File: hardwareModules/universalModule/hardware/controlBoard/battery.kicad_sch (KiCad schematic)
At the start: 36 parts, among them Q1 AONR21357, Q2 AONR21357, Q3 2N7002, U10 TP5100, U4 SD8942, U9 PIEZO

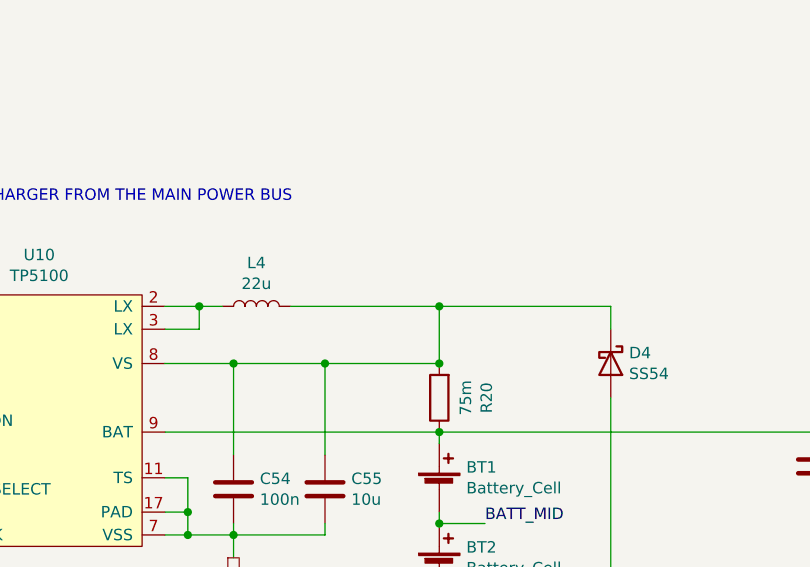
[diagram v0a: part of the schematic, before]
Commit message: um: Fix hardware bugs, prepare v0.5
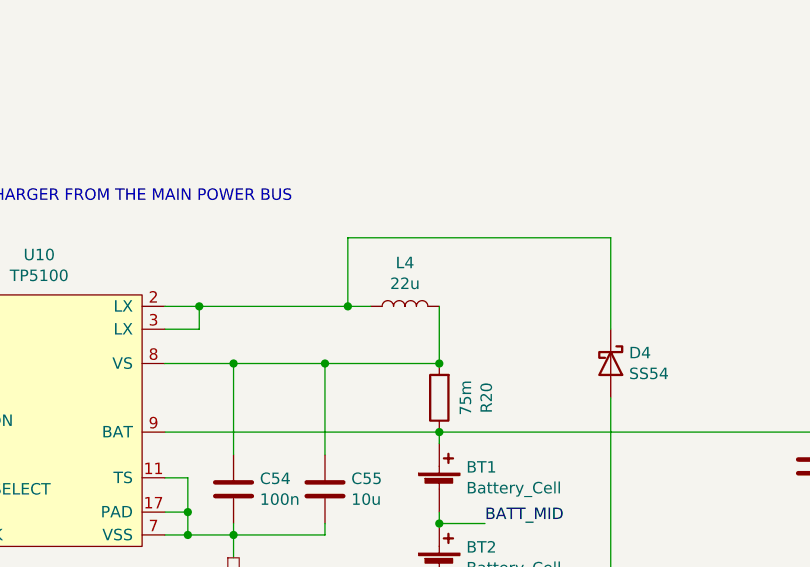
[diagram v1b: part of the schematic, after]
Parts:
- U4: JLCPCB_CORRECTION 0;0;180 -> 0;0;-90
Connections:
- net at L4.1, U10.2 (LX), U10.3 (LX): now also D4.1 (K)
- net at C54.1, C55.1, L4.2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: no longer D4.1 (K)
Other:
- moved on the sheet: L4
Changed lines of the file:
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@@
 (kicad_sch (version 20211123) (generator eeschema)
   (paper "A4")
-  (junction (at 130.81 81.28) (diameter 0) (color 0 0 0 0)
-  )
   (junction (at 104.14 81.28) (diameter 0) (color 0 0 0 0)
   )
@@
   )
   (junction (at 130.81 105.41) (diameter 0) (color 0 0 0 0)
+  )
+  (junction (at 120.65 81.28) (diameter 0) (color 0 0 0 0)
   )
   (junction (at 130.81 118.11) (diameter 0) (color 0 0 0 0)
@@
     (stroke (width 0) (type default) (color 0 0 0 0))
   )
-  (wire (pts (xy 149.86 81.28) (xy 149.86 83.82))
+  (wire (pts (xy 149.86 73.66) (xy 149.86 83.82))
     (stroke (width 0) (type default) (color 0 0 0 0))
   )
@@
     (stroke (width 0) (type default) (color 0 0 0 0))
   )
-  (wire (pts (xy 114.3 81.28) (xy 130.81 81.28))
-    (stroke (width 0) (type default) (color 0 0 0 0))
-  )
   (wire (pts (xy 220.98 44.45) (xy 242.57 44.45))
     (stroke (width 0) (type default) (color 0 0 0 0))
@@
     (stroke (width 0) (type default) (color 0 0 0 0))
   )
-  (wire (pts (xy 104.14 81.28) (xy 106.68 81.28))
+  (wire (pts (xy 104.14 81.28) (xy 120.65 81.28))
     (stroke (width 0) (type default) (color 0 0 0 0))
   )
@@
     (stroke (width 0) (type default) (color 0 0 0 0))
   )
-  (wire (pts (xy 130.81 81.28) (xy 149.86 81.28))
-    (stroke (width 0) (type default) (color 0 0 0 0))
-  )
   (wire (pts (xy 100.33 100.33) (xy 102.87 100.33))
     (stroke (width 0) (type default) (color 0 0 0 0))
@@
     (stroke (width 0) (type default) (color 0 0 0 0))
   )
+  (wire (pts (xy 120.65 73.66) (xy 120.65 81.28))
+    (stroke (width 0) (type default) (color 0 0 0 0))
+  )
   (wire (pts (xy 130.81 113.03) (xy 130.81 114.3))
     (stroke (width 0) (type default) (color 0 0 0 0))
   )
+  (wire (pts (xy 149.86 73.66) (xy 120.65 73.66))
+    (stroke (width 0) (type default) (color 0 0 0 0))
+  )
   (wire (pts (xy 130.81 114.3) (xy 130.81 118.11))
     (stroke (width 0) (type default) (color 0 0 0 0))
@@
   )
   (wire (pts (xy 80.01 162.56) (xy 80.01 165.1))
+    (stroke (width 0) (type default) (color 0 0 0 0))
+  )
+  (wire (pts (xy 120.65 81.28) (xy 123.19 81.28))
     (stroke (width 0) (type default) (color 0 0 0 0))
   )
@@
     (pin "9")
   )
-  (symbol (lib_id "Device:L") (at 110.49 81.28 90) (unit 1)
-    (in_bom yes) (on_board yes)
-    (property "Reference" "L4" (id 0) (at 110.49 76.454 90))
-    (property "Value" "22u" (id 1) (at 110.49 78.7654 90))
-    (property "Footprint" "rofi:SLO0630H" (id 2) (at 110.49 81.28 0)
-      (effects (font (size 1.27 1.27)) hide)
-    )
-    (property "Datasheet" "~" (id 3) (at 110.49 81.28 0)
-      (effects (font (size 1.27 1.27)) hide)
-    )
-    (property "LCSC" "C207843" (id 4) (at 110.49 81.28 90)
+  (symbol (lib_id "Device:L") (at 127 81.28 90) (unit 1)
+    (in_bom yes) (on_board yes)
+    (property "Reference" "L4" (id 0) (at 127 76.454 90))
+    (property "Value" "22u" (id 1) (at 127 78.7654 90))
+    (property "Footprint" "rofi:SLO0630H" (id 2) (at 127 81.28 0)
+      (effects (font (size 1.27 1.27)) hide)
+    )
+    (property "Datasheet" "~" (id 3) (at 127 81.28 0)
+      (effects (font (size 1.27 1.27)) hide)
+    )
+    (property "LCSC" "C207843" (id 4) (at 127 81.28 90)
       (effects (font (size 1.27 1.27)) hide)
     )
@@
       (effects (font (size 1.27 1.27)) hide)
     )
-    (property "JLCPCB_CORRECTION" "0;0;180" (id 5) (at 95.25 154.94 0)
-      (effects (font (size 1.27 1.27)) hide)
-    )
+    (property "JLCPCB_CORRECTION" "0;0;-90" (id 5) (at 95.25 154.94 0)
+      (effects (font (size 1.27 1.27)) hide)
+    )

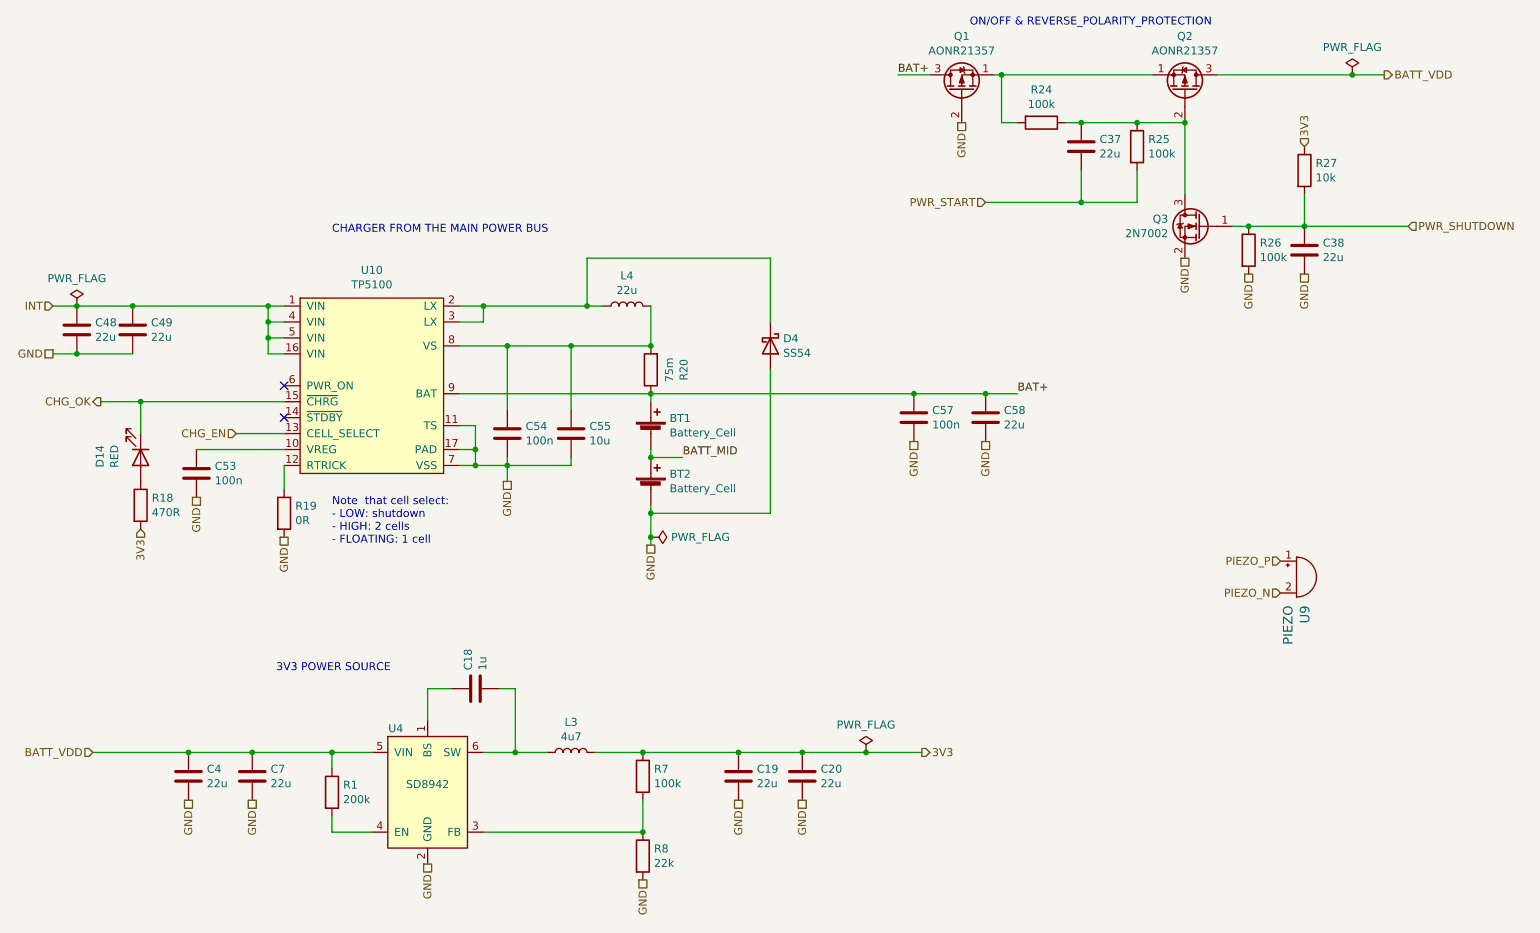
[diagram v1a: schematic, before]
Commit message: hardware: Add custom FPC cables
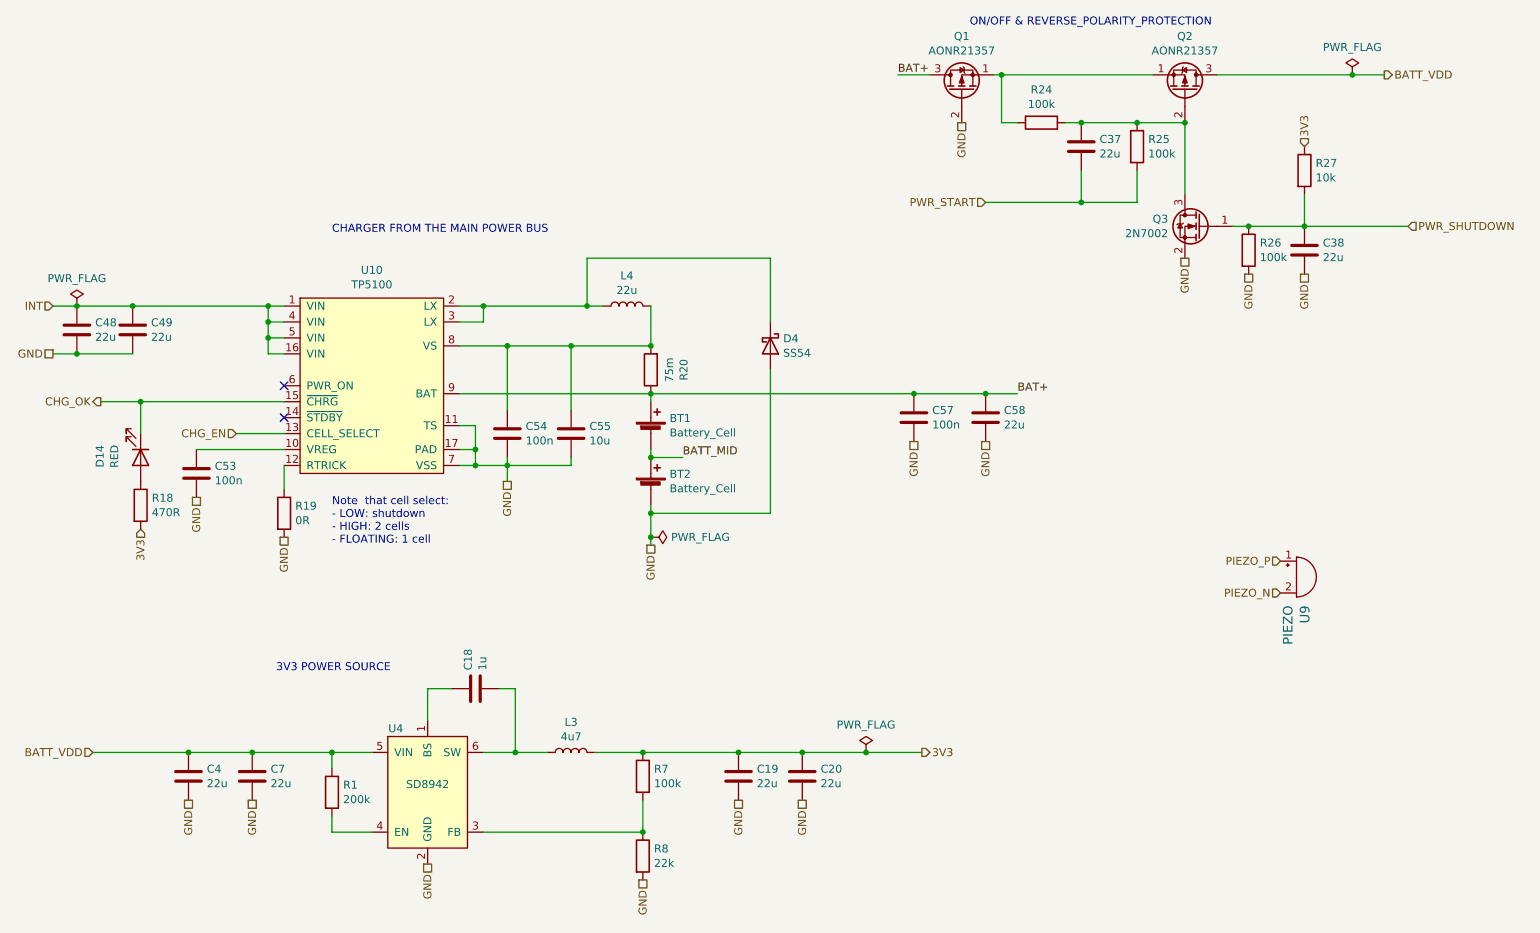
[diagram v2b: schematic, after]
